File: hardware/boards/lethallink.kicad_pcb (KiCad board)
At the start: 6 copper layers, 86 x 111.1 mm, 104 parts, among them J1 PCIe-x4, J2 USB3_Micro_B_Amphenol, Q1 Q_NMOS_GSD, Q2 Q_NMOS_GSD, Q3 Q_NMOS_GSD, Q4 Q_NMOS_GSD, Q5 SI7232DN-T1-GE3, SW1 SW_DIP_x03, U1 ECP5UM5G-381caBGA, U2 ADP5050ACPZ-R7, U3 CYUSB3014, U4 IS43TR16256B-125KBL

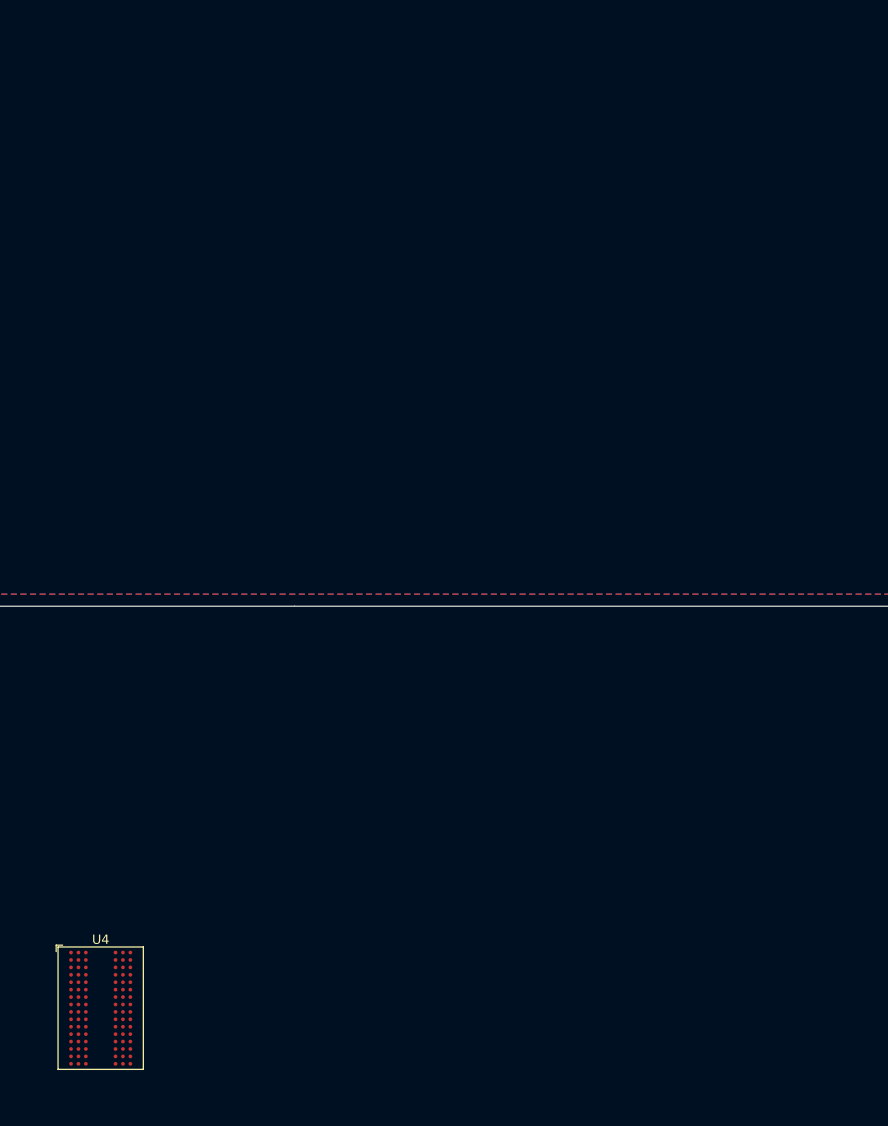
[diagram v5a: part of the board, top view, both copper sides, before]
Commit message: Added the SPI Flash for the gateware, softcore firmware, and USB controller firmware, all the firmware really.
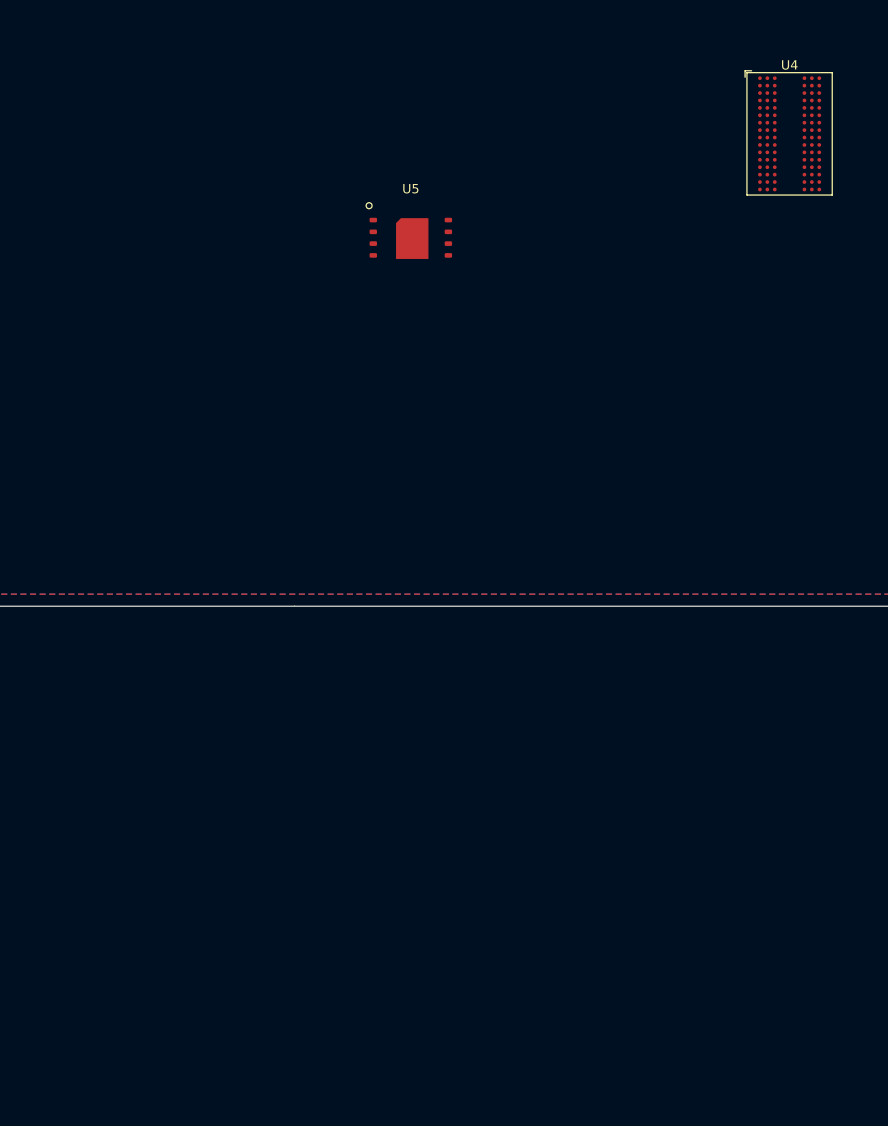
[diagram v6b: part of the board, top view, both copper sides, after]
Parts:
- added U5: 128MiB, lethalbit-memory:WSON-8-1EP-6.0x8.0mm, F.Cu at (116.0, -24.0)
- moved U4 120.1 mm to (156.8, -35.2)
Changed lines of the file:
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@@
     (tracks 10)
     (zones 0)
-    (modules 104)
-    (nets 512)
+    (modules 105)
+    (nets 520)
   )
   (page A3)
@@
   (net 510 "Net-(U4-PadA3)")
   (net 511 "Net-(U4-PadA2)")
+  (net 512 "Net-(U5-Pad4)")
+  (net 513 "Net-(U5-Pad7)")
+  (net 514 "Net-(U5-Pad5)")
+  (net 515 "Net-(U5-Pad6)")
+  (net 516 "Net-(U5-Pad8)")
+  (net 517 "Net-(U5-Pad3)")
+  (net 518 "Net-(U5-Pad2)")
+  (net 519 "Net-(U5-Pad1)")
   (net_class Default "This is the default net class."
     (clearance 0.2)
@@
     (add_net "Net-(U4-PadT7)")
     (add_net "Net-(U4-PadT8)")
+    (add_net "Net-(U5-Pad1)")
+    (add_net "Net-(U5-Pad2)")
+    (add_net "Net-(U5-Pad3)")
+    (add_net "Net-(U5-Pad4)")
+    (add_net "Net-(U5-Pad5)")
+    (add_net "Net-(U5-Pad6)")
+    (add_net "Net-(U5-Pad7)")
+    (add_net "Net-(U5-Pad8)")
+  )
+  (module lethalbit-memory:WSON-8-1EP-6.0x8.0mm (layer F.Cu)
+    (at 116 -24)
+    (fp_text reference U5 (at 0 -5.3) (layer F.SilkS)
+      (effects (font (size 1 1) (thickness 0.15)))
+    )
+    (fp_text value 128MiB (at -0.1 -9.85) (layer F.Fab)
+      (effects (font (size 1 1) (thickness 0.15)))
+    )
+    (fp_circle (center -4.5 -3.5) (end -4.75 -3.7) (layer F.SilkS) (width 0.12))
+    (fp_line (start -5 -4) (end 5 -4) (layer F.CrtYd) (width 0.12))
+    (fp_line (start 5 -4) (end 5 4) (layer F.CrtYd) (width 0.12))
+    (fp_line (start 5 4) (end -5 4) (layer F.CrtYd) (width 0.12))
+    (fp_line (start -5 4) (end -5 -4) (layer F.CrtYd) (width 0.12))
+    (pad 9 smd custom (at 0 0) (size 0.7 0.7) (layers F.Cu F.Paste F.Mask)
+      (net 512 "Net-(U5-Pad4)") (zone_connect 0)
+      (options (clearance outline) (anchor circle))
+      (primitives
+        (gr_poly (pts
+           (xy -1.55 -1.6) (xy -1.55 2.2) (xy 1.85 2.2) (xy 1.85 -2.1) (xy -1.05 -2.1)
+           (xy -1.3 -1.85)) (width 0.1))
+      ))
+    (pad 7 smd roundrect (at 4.05 -0.68) (size 0.8 0.5) (layers F.Cu F.Paste F.Mask) (roundrect_rratio 0.25)
+      (net 513 "Net-(U5-Pad7)"))
+    (pad 5 smd roundrect (at 4.05 1.86) (size 0.8 0.5) (layers F.Cu F.Paste F.Mask) (roundrect_rratio 0.25)
+      (net 514 "Net-(U5-Pad5)"))
+    (pad 6 smd roundrect (at 4.05 0.59) (size 0.8 0.5) (layers F.Cu F.Paste F.Mask) (roundrect_rratio 0.25)
+      (net 515 "Net-(U5-Pad6)"))
+    (pad 8 smd roundrect (at 4.05 -1.95) (size 0.8 0.5) (layers F.Cu F.Paste F.Mask) (roundrect_rratio 0.25)
+      (net 516 "Net-(U5-Pad8)"))
+    (pad 4 smd roundrect (at -4.05 1.86) (size 0.8 0.5) (layers F.Cu F.Paste F.Mask) (roundrect_rratio 0.25)
+      (net 512 "Net-(U5-Pad4)"))
+    (pad 3 smd roundrect (at -4.05 0.59) (size 0.8 0.5) (layers F.Cu F.Paste F.Mask) (roundrect_rratio 0.25)
+      (net 517 "Net-(U5-Pad3)"))
+    (pad 2 smd roundrect (at -4.05 -0.68) (size 0.8 0.5) (layers F.Cu F.Paste F.Mask) (roundrect_rratio 0.25)
+      (net 518 "Net-(U5-Pad2)"))
+    (pad 1 smd roundrect (at -4.05 -1.95) (size 0.8 0.5) (layers F.Cu F.Paste F.Mask) (roundrect_rratio 0.25)
+      (net 519 "Net-(U5-Pad1)"))
+    (model ${KISYS3DMOD}/Package_SON.3dshapes/WSON-8-1EP_3x3mm_P0.5mm_EP1.6x2.0mm.wrl
+      (at (xyz 0 0 0))
+      (scale (xyz 2.9 2.5 1))
+      (rotate (xyz 0 0 0))
+    )
   )
   (module Package_BGA:BGA-96_9.0x13.0mm_Layout2x3x16_P0.8mm (layer F.Cu)
-    (at 82.55 59.05)
+    (at 156.85 -35.25)
     (descr "BGA-96, http://www.mouser.com/ds/2/198/43-46TR16640B-81280BL-706483.pdf")
     (tags BGA-96)

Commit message: Got a fair bit of the initial layout done for the power supply
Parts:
- moved D3 174.8 mm to (99.9, 181.4)
- moved D1 168.0 mm to (99.9, 176.5)
- moved R2 167.8 mm to (104.8, 172.2), turned to 180 degrees
- moved R3 163.1 mm to (104.9, 181.7), turned to 180 degrees
- moved D2 156.4 mm to (99.5, 172.2)
- moved R1 156.3 mm to (104.7, 176.6), turned to 180 degrees
- moved C6 122.8 mm to (173.8, 200.2), turned to 180 degrees
- moved R31 122.6 mm to (154.5, 209.0)
- moved R10 122.1 mm to (165.5, 198.0), turned to 180 degrees
- moved R32 121.8 mm to (147.8, 137.8)
- moved D5 120.0 mm to (158.5, 209.0), turned to 180 degrees
- moved Q1 118.7 mm to (163.0, 208.8), turned to 180 degrees
- moved R29 112.6 mm to (166.5, 209.8), turned to 180 degrees
- moved R16 111.2 mm to (163.8, 146.8)
- moved R5 107.9 mm to (174.8, 202.8), turned to 270 degrees
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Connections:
- Q5 pad 3: Net-(C16-Pad2) -> Net-(C15-Pad2)
- Q5 pad 6: Net-(C15-Pad2) -> Net-(C16-Pad2)
- U2 pad 29: Net-(Q5-Pad5) -> Net-(Q5-Pad2)
- U2 pad 31: Net-(Q5-Pad2) -> Net-(Q5-Pad5)
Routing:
- net Net-(Q5-Pad2): track 0.00 -> 15.7 mm, vias 0 -> 2
- net Net-(Q5-Pad5): track 0.00 -> 13.9 mm, vias 0 -> 2
- net Net-(C16-Pad1): track 0.00 -> 3.89 mm
- net Net-(C15-Pad1): track 0.00 -> 3.81 mm
- added copper zone on F.Cu, net +12V
- added copper zone on F.Cu, net +1V2
- added copper zone on F.Cu, net +1V5
- added copper zone on F.Cu, net Net-(C15-Pad2)
- added copper zone on F.Cu, net Net-(C16-Pad2)
